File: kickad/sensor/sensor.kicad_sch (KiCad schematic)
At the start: 13 parts, among them J3 trackball, U2 PMW3610

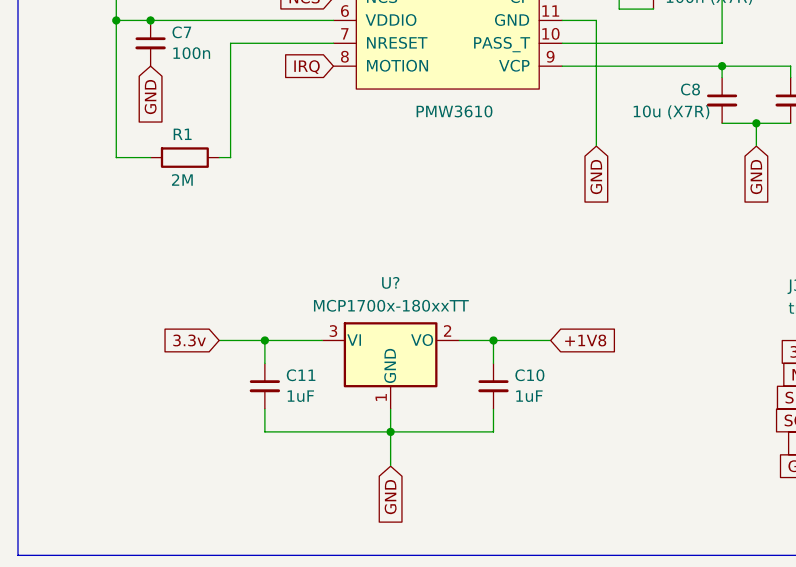
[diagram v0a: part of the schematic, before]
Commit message: Reworking the sensor PCB
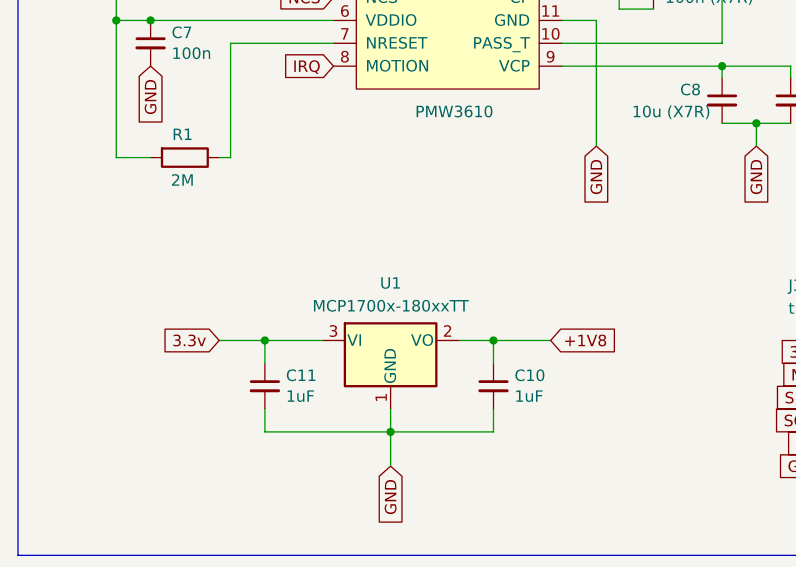
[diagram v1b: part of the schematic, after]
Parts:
- gave numbers to parts that had none: 1
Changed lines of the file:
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@@
 		(dnp no)
 		(fields_autoplaced yes)
-		(property "Reference" "U?"
+		(property "Reference" "U1"
 			(at 60.96 241.3 0)
 			(effects
@@
 			(project ""
 				(path "/3a835e6f-a660-4b38-a102-87841cdd95ed"
-					(reference "U?")
+					(reference "U1")
 					(unit 1)
 				)

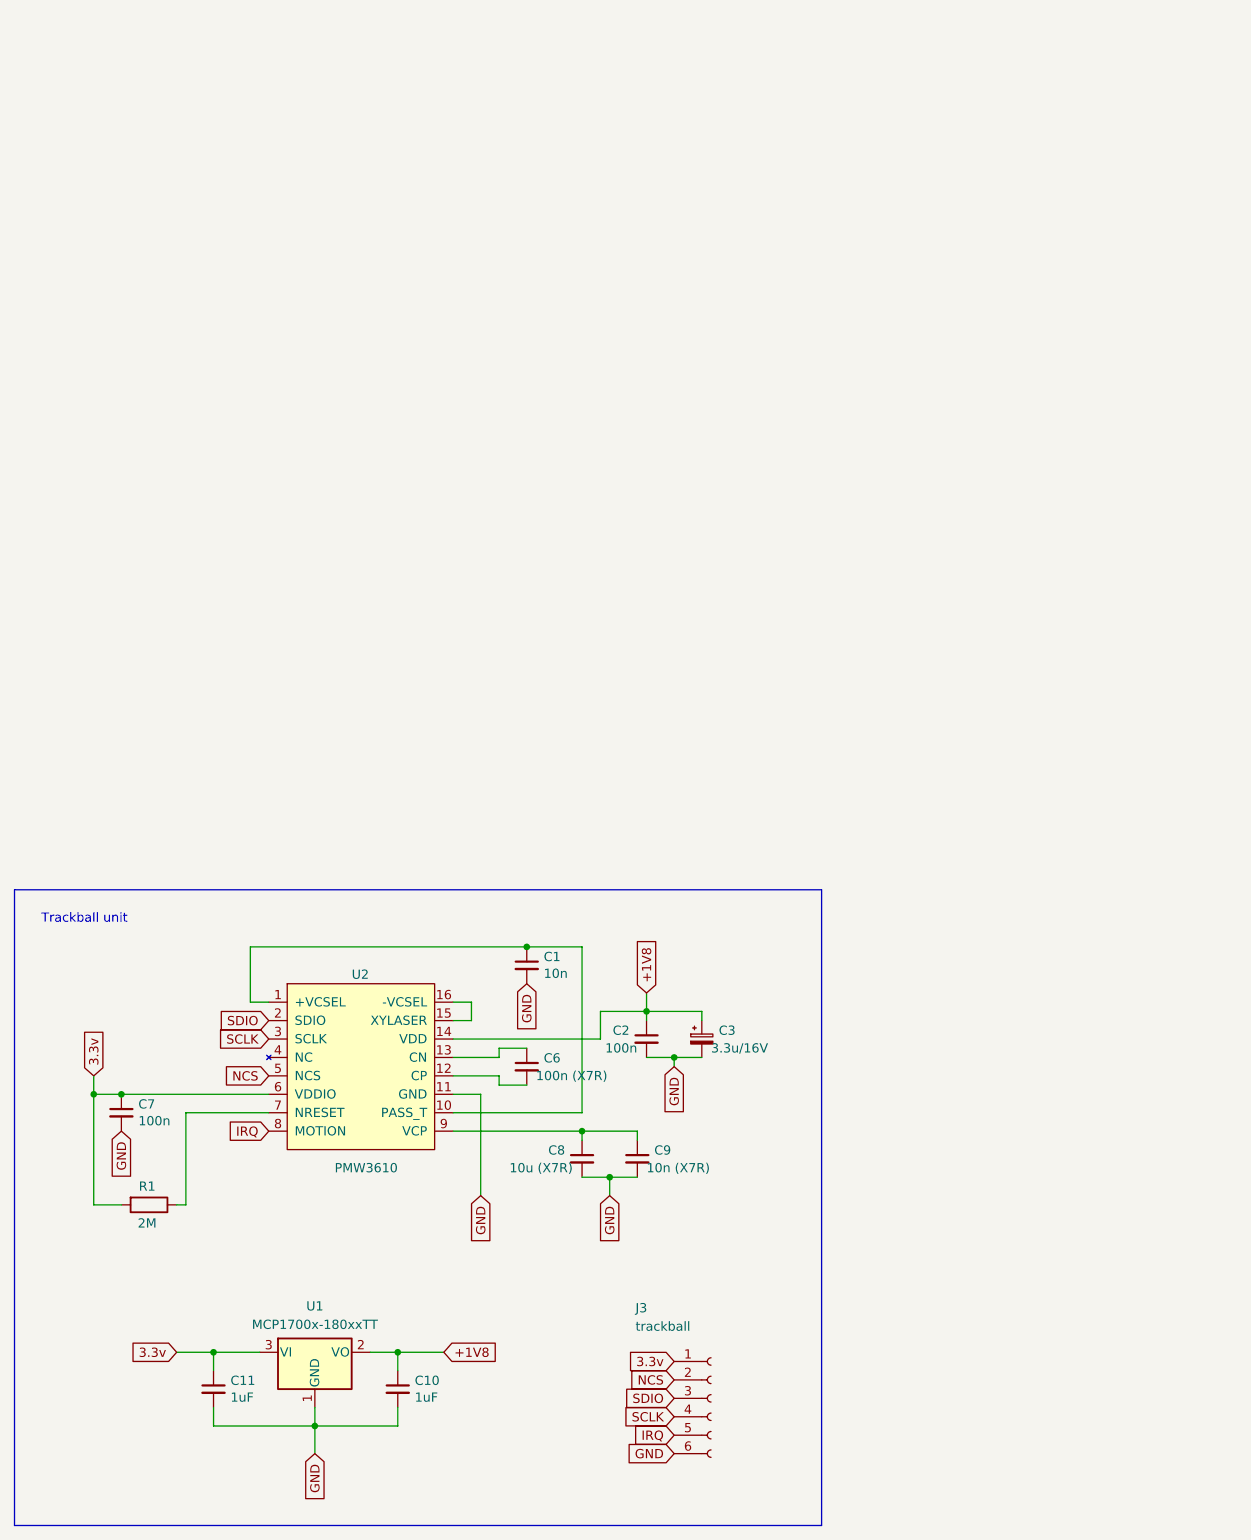
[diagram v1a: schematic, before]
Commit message: Resetting the mobo stack to 4 layers mirrorable
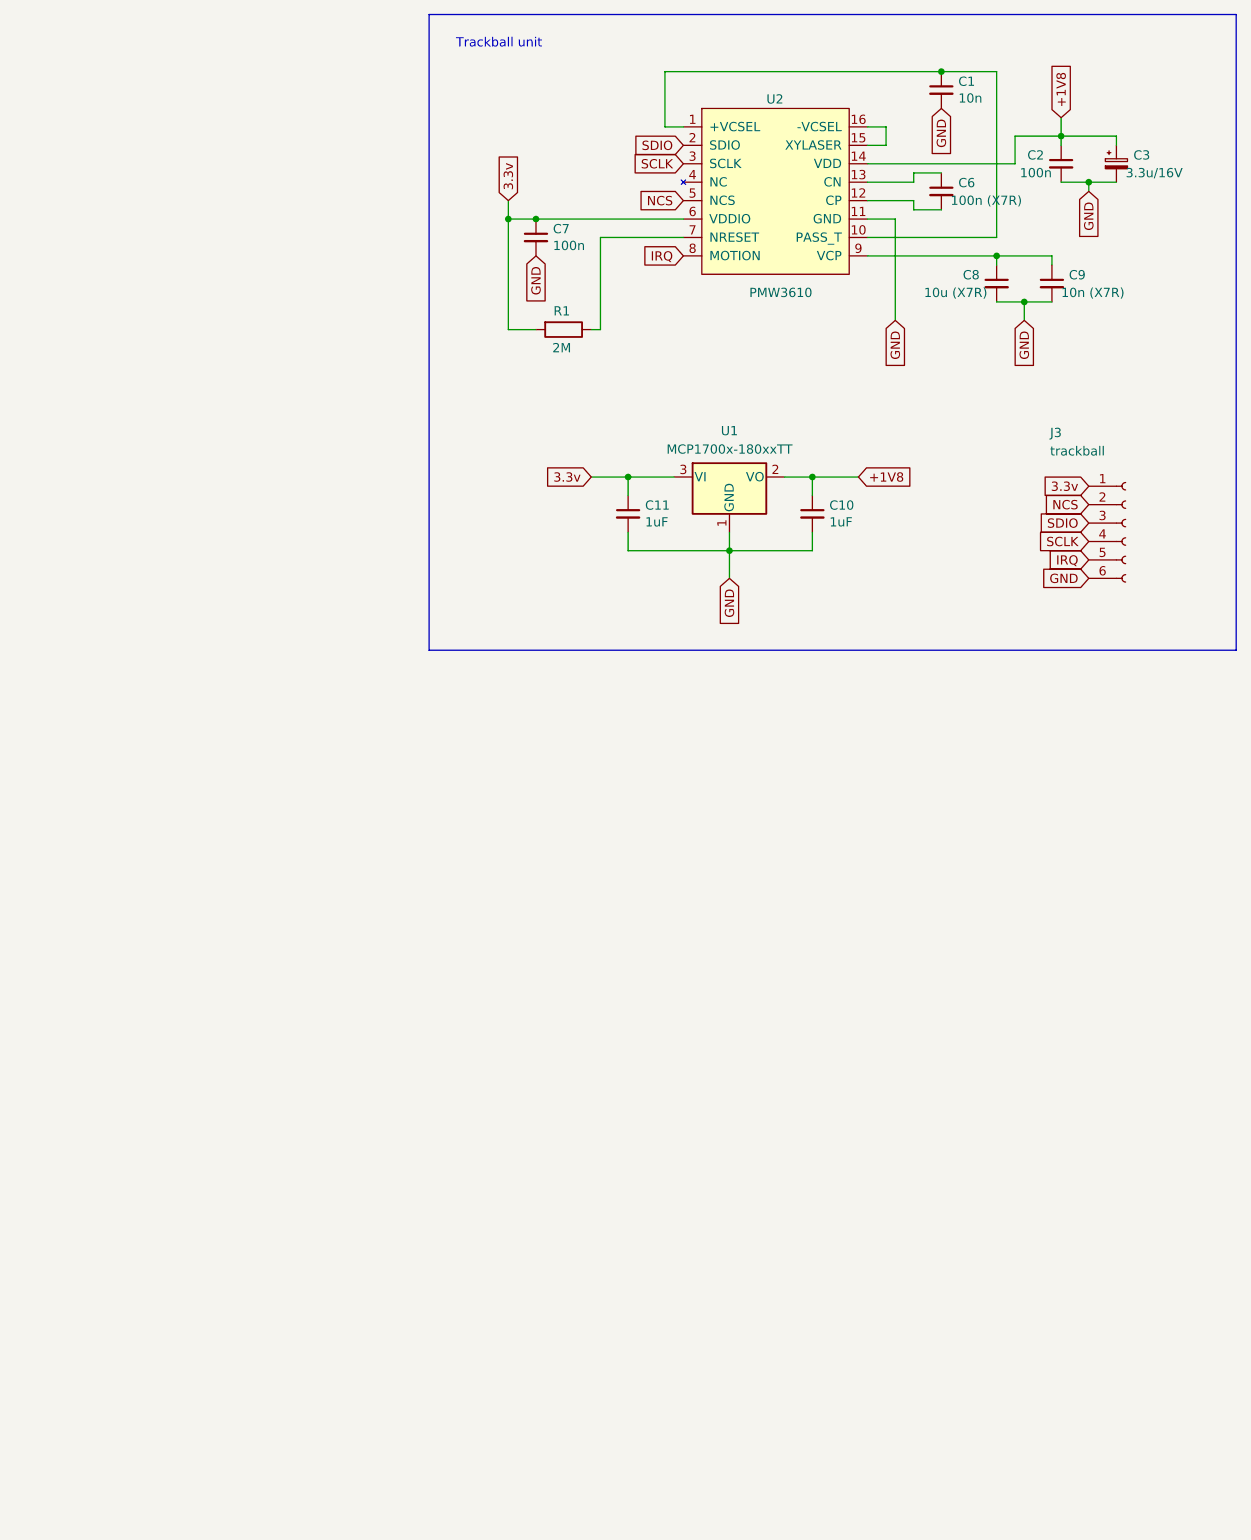
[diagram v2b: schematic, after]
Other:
- moved on the sheet: C1, C10, C11, C2, C3, C6, C7, C8, C9, J3, R1, U1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
